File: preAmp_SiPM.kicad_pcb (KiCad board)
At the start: 2 copper layers, 15 parts, among them J3 Conn_01x02_Pin, J4 Conn_01x02_Pin, J5 Conn_01x02_Pin, J6 Conn_01x02_Pin, Q1 BFR92

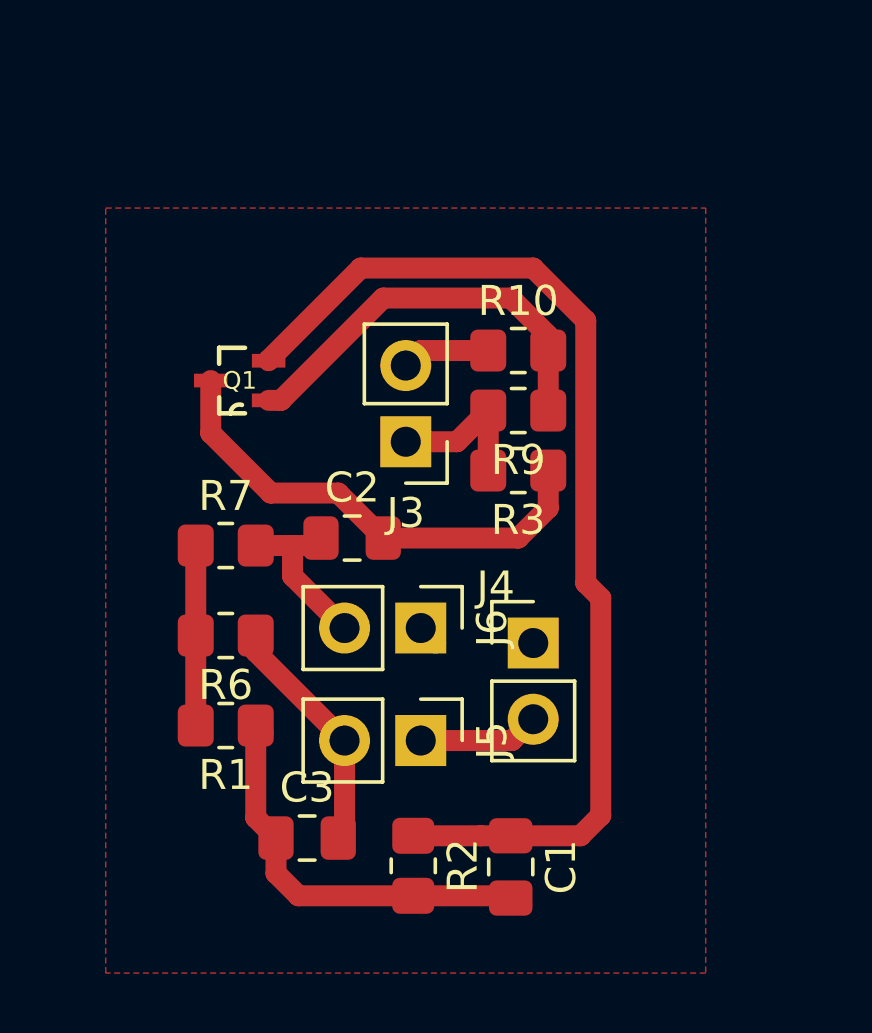
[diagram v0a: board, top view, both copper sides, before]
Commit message: Adding a Capacitor and Design again the PCB
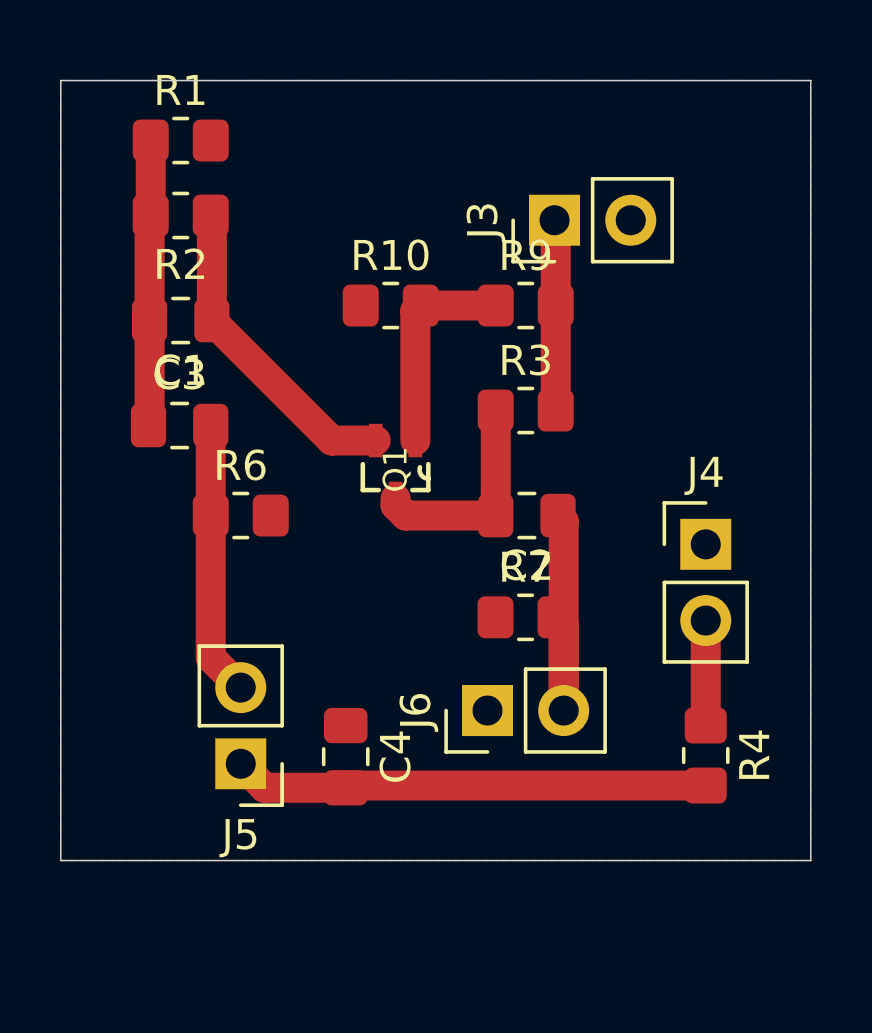
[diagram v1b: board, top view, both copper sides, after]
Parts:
- added C4: C, Capacitor_SMD:C_0805_2012Metric_Pad1.18x1.45mm_HandSolder, F.Cu at (160.0, 76.5)
- added R4: R_US, Resistor_SMD:R_0805_2012Metric_Pad1.20x1.40mm_HandSolder, F.Cu at (172.0, 76.5)
- moved R2 23.0 mm to (154.5, 58.5), turned to 180 degrees
- moved C1 21.3 mm to (154.5, 62.0), turned to 180 degrees
- moved R1 19.6 mm to (154.5, 56.0), turned to 0 degrees
- moved C3 14.4 mm to (154.5, 65.5)
- moved R7 10.3 mm to (166.0, 71.9)
- moved J3 8.89 mm to (167.0, 58.7), turned to 90 degrees
- moved J4 6.62 mm to (172.0, 69.5)
- moved J5 6.05 mm to (156.5, 76.8), turned to 180 degrees
- moved Q1 5.98 mm to (161.7, 67.0), turned to -90 degrees
- moved C2 5.87 mm to (166.0, 68.5), turned to 180 degrees
- moved R10 4.51 mm to (161.5, 61.5)
- moved R6 4.03 mm to (156.5, 68.5), turned to 0 degrees
- moved J6 3.54 mm to (164.7, 75.0), turned to 90 degrees
- moved R9 3.51 mm to (166.0, 61.5), turned to 0 degrees
- moved R3 2.02 mm to (166.0, 65.0), turned to 0 degrees
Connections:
- J5 pad 1: Net-(J4-Pin_2) -> Net-(J5-Pin_1)
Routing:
- net Net-(Q1-E): track 35.8 -> 10.6 mm
- net Net-(J5-Pin_1): track 0.00 -> 15.9 mm
- net GND: track 9.66 -> 0.00 mm
- net Net-(Q1-C): track 16.1 -> 7.21 mm
- net Net-(Q1-B): track 13.8 -> 7.07 mm
- net Net-(C1-Pad2): track 13.7 -> 9.58 mm
- net Net-(J6-Pin_2): track 5.75 -> 9.80 mm
- net Net-(J3-Pin_1): track 5.18 -> 6.36 mm
- net Net-(J5-Pin_2): track 8.06 -> 9.15 mm
- net Net-(J4-Pin_2): track 4.04 -> 3.50 mm
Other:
- board outline added: 25 x 26 mm
